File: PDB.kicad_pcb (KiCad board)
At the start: 2 copper layers, 63 parts, among them J1 Conn_02x03_Odd_Even, J2 USB_C_Receptacle_USB2.0, U1 ATmega2560-16AU, U2 LMZ13608, U3 LTC2946, U4 LTC2946, U5 FT230XQ, U6 Si8621, Y1 16MHz

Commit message: layout WIP
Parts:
- added C23: XT-F, XT30:XT30PW-F, F.Cu at (181.5, 66.5)
- added C24: XT-F, XT30:XT30PW-F, F.Cu at (199.0, 65.5)
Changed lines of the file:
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@@
     (tracks 177)
     (zones 0)
-    (modules 63)
+    (modules 65)
     (nets 138)
   )
@@
     (add_net "Net-(U5-Pad9)")
   )
+  (module XT30:XT30PW-F (layer F.Cu)
+    (at 199 65.5)
+    (fp_text reference C24 (at 0 18) (layer F.SilkS)
+      (effects (font (size 1 1) (thickness 0.15)))
+    )
+    (fp_text value XT-F (at 0 10) (layer F.Fab)
+      (effects (font (size 1 1) (thickness 0.15)))
+    )
+    (fp_line (start 4.5 6) (end 4.95 6) (layer F.Fab) (width 0.05))
+    (fp_line (start 4.5 0) (end 4.5 6) (layer F.Fab) (width 0.05))
+    (fp_line (start -4.5 6) (end -4.95 6) (layer F.Fab) (width 0.05))
+    (fp_line (start -4.5 0) (end -4.5 6) (layer F.Fab) (width 0.05))
+    (fp_text user REF** (at 0 8.5) (layer F.Fab)
+      (effects (font (size 1 1) (thickness 0.15)))
+    )
+    (fp_line (start 5 13) (end 5 17.1) (layer F.CrtYd) (width 0.05))
+    (fp_line (start 6.75 13) (end 5 13) (layer F.CrtYd) (width 0.05))
+    (fp_line (start -5 13) (end -6.75 13) (layer F.CrtYd) (width 0.05))
+    (fp_line (start -5 17.1) (end -5 13) (layer F.CrtYd) (width 0.05))
+    (fp_line (start -4.95 7.9) (end -5.5 7.9) (layer F.Fab) (width 0.05))
+    (fp_line (start -4.95 10.2) (end -5.5 10.2) (layer F.Fab) (width 0.05))
+    (fp_arc (start -5.5 9.05) (end -5.5 7.9) (angle -180) (layer F.Fab) (width 0.05))
+    (fp_line (start 4.95 10.2) (end 5.5 10.2) (layer F.Fab) (width 0.05))
+    (fp_line (start 4.95 7.9) (end 5.5 7.9) (layer F.Fab) (width 0.05))
+    (fp_arc (start 5.5 9.05) (end 5.5 10.2) (angle -180) (layer F.Fab) (width 0.05))
+    (fp_arc (start 2.5 14.05) (end 1.65 14.05) (angle -180) (layer F.Fab) (width 0.05))
+    (fp_arc (start -2.5 14.05) (end -3.35 14.05) (angle -180) (layer F.Fab) (width 0.05))
+    (fp_line (start 3.35 11) (end 3.35 14.05) (layer F.Fab) (width 0.05))
+    (fp_line (start 1.65 11) (end 1.65 14.05) (layer F.Fab) (width 0.05))
+    (fp_line (start -1.65 11) (end -1.65 14.05) (layer F.Fab) (width 0.05))
+    (fp_line (start -3.35 11) (end -3.35 14.05) (layer F.Fab) (width 0.05))
+    (fp_line (start -4.95 11) (end -4.95 6) (layer F.Fab) (width 0.05))
+    (fp_line (start 4.95 11) (end -4.95 11) (layer F.Fab) (width 0.05))
+    (fp_line (start 4.95 6) (end 4.95 11) (layer F.Fab) (width 0.05))
+    (fp_line (start -4.5 0) (end 4.5 0) (layer F.Fab) (width 0.05))
+    (fp_line (start -6.75 13) (end -6.75 -0.5) (layer F.CrtYd) (width 0.05))
+    (fp_line (start 5 17.1) (end -5 17.1) (layer F.CrtYd) (width 0.05))
+    (fp_line (start 6.75 -0.5) (end 6.75 13) (layer F.CrtYd) (width 0.05))
+    (fp_line (start -6.75 -0.5) (end 6.75 -0.5) (layer F.CrtYd) (width 0.05))
+    (pad 4 thru_hole circle (at 5.5 9.05) (size 2 2) (drill 1) (layers *.Cu *.Mask)
+      (net 1 GND))
+    (pad 3 thru_hole circle (at -5.5 9.05) (size 2 2) (drill 1) (layers *.Cu *.Mask)
+      (net 1 GND))
+    (pad 1 thru_hole circle (at 2.5 14.05) (size 3 3) (drill 1.7) (layers *.Cu *.Mask)
+      (net 43 +5V))
+    (pad 2 thru_hole circle (at -2.5 14.05) (size 3 3) (drill 1.7) (layers *.Cu *.Mask)
+      (net 1 GND))
+    (model ${KIPRJMOD}/ottojo_KicadLibs/XT30.pretty/XT30PW-F.stp
+      (offset (xyz 0 -8.300000000000001 0))
+      (scale (xyz 1 1 1))
+      (rotate (xyz 0 0 90))
+    )
+  )
+  (module XT30:XT30PW-F (layer F.Cu)
+    (at 181.5 66.5)
+    (fp_text reference C23 (at 0 18) (layer F.SilkS)
+      (effects (font (size 1 1) (thickness 0.15)))
+    )
+    (fp_text value XT-F (at 0 10) (layer F.Fab)
+      (effects (font (size 1 1) (thickness 0.15)))
+    )
+    (fp_line (start 4.5 6) (end 4.95 6) (layer F.Fab) (width 0.05))
+    (fp_line (start 4.5 0) (end 4.5 6) (layer F.Fab) (width 0.05))
+    (fp_line (start -4.5 6) (end -4.95 6) (layer F.Fab) (width 0.05))
+    (fp_line (start -4.5 0) (end -4.5 6) (layer F.Fab) (width 0.05))
+    (fp_text user REF** (at 0 8.5) (layer F.Fab)
+      (effects (font (size 1 1) (thickness 0.15)))
+    )
+    (fp_line (start 5 13) (end 5 17.1) (layer F.CrtYd) (width 0.05))
+    (fp_line (start 6.75 13) (end 5 13) (layer F.CrtYd) (width 0.05))
+    (fp_line (start -5 13) (end -6.75 13) (layer F.CrtYd) (width 0.05))
+    (fp_line (start -5 17.1) (end -5 13) (layer F.CrtYd) (width 0.05))
+    (fp_line (start -4.95 7.9) (end -5.5 7.9) (layer F.Fab) (width 0.05))
+    (fp_line (start -4.95 10.2) (end -5.5 10.2) (layer F.Fab) (width 0.05))
+    (fp_arc (start -5.5 9.05) (end -5.5 7.9) (angle -180) (layer F.Fab) (width 0.05))
+    (fp_line (start 4.95 10.2) (end 5.5 10.2) (layer F.Fab) (width 0.05))
+    (fp_line (start 4.95 7.9) (end 5.5 7.9) (layer F.Fab) (width 0.05))
+    (fp_arc (start 5.5 9.05) (end 5.5 10.2) (angle -180) (layer F.Fab) (width 0.05))
+    (fp_arc (start 2.5 14.05) (end 1.65 14.05) (angle -180) (layer F.Fab) (width 0.05))
+    (fp_arc (start -2.5 14.05) (end -3.35 14.05) (angle -180) (layer F.Fab) (width 0.05))
+    (fp_line (start 3.35 11) (end 3.35 14.05) (layer F.Fab) (width 0.05))
+    (fp_line (start 1.65 11) (end 1.65 14.05) (layer F.Fab) (width 0.05))
+    (fp_line (start -1.65 11) (end -1.65 14.05) (layer F.Fab) (width 0.05))
+    (fp_line (start -3.35 11) (end -3.35 14.05) (layer F.Fab) (width 0.05))
+    (fp_line (start -4.95 11) (end -4.95 6) (layer F.Fab) (width 0.05))
+    (fp_line (start 4.95 11) (end -4.95 11) (layer F.Fab) (width 0.05))
+    (fp_line (start 4.95 6) (end 4.95 11) (layer F.Fab) (width 0.05))
+    (fp_line (start -4.5 0) (end 4.5 0) (layer F.Fab) (width 0.05))
+    (fp_line (start -6.75 13) (end -6.75 -0.5) (layer F.CrtYd) (width 0.05))
+    (fp_line (start 5 17.1) (end -5 17.1) (layer F.CrtYd) (width 0.05))
+    (fp_line (start 6.75 -0.5) (end 6.75 13) (layer F.CrtYd) (width 0.05))
+    (fp_line (start -6.75 -0.5) (end 6.75 -0.5) (layer F.CrtYd) (width 0.05))
+    (pad 4 thru_hole circle (at 5.5 9.05) (size 2 2) (drill 1) (layers *.Cu *.Mask)
+      (net 1 GND))
+    (pad 3 thru_hole circle (at -5.5 9.05) (size 2 2) (drill 1) (layers *.Cu *.Mask)
+      (net 1 GND))
+    (pad 1 thru_hole circle (at 2.5 14.05) (size 3 3) (drill 1.7) (layers *.Cu *.Mask)
+      (net 43 +5V))
+    (pad 2 thru_hole circle (at -2.5 14.05) (size 3 3) (drill 1.7) (layers *.Cu *.Mask)
+      (net 1 GND))
+    (model ${KIPRJMOD}/ottojo_KicadLibs/XT30.pretty/XT30PW-F.stp
+      (offset (xyz 0 -8.300000000000001 0))
+      (scale (xyz 1 1 1))
+      (rotate (xyz 0 0 90))
+    )
+  )
   (module XT60:XT60PW-F (layer F.Cu)
     (at 98 65)
@@
       (effects (font (size 1 1) (thickness 0.15)))
     )
+    (fp_line (start -5 -1.75) (end 5 -1.75) (layer F.Fab) (width 0.1))
+    (fp_line (start -8 9) (end -8 -11) (layer F.CrtYd) (width 0.05))
+    (fp_line (start 8 9) (end -8 9) (layer F.CrtYd) (width 0.05))
+    (fp_line (start 8 -11) (end 8 9) (layer F.CrtYd) (width 0.05))
     (fp_line (start -8 -11) (end 8 -11) (layer F.CrtYd) (width 0.05))
-    (fp_line (start 8 -11) (end 8 9) (layer F.CrtYd) (width 0.05))
-    (fp_line (start 8 9) (end -8 9) (layer F.CrtYd) (width 0.05))
-    (fp_line (start -8 9) (end -8 -11) (layer F.CrtYd) (width 0.05))
-    (fp_line (start -5 -1.75) (end 5 -1.75) (layer F.Fab) (width 0.1))
-    (pad 4 thru_hole oval (at 6.75 0 90) (size 2.9 1.3) (drill oval 2.3 0.7) (layers *.Cu *.Mask)
-      (net 1 GND))
-    (pad 3 thru_hole oval (at -6.75 0 90) (size 2.9 1.3) (drill oval 2.3 0.7) (layers *.Cu *.Mask)
-      (net 1 GND))
-    (pad 2 thru_hole circle (at 3.6 6 90) (size 4.5 4.5) (drill 2.8) (layers *.Cu *.Mask)
-      (net 1 GND))
     (pad 1 thru_hole circle (at -3.6 6) (size 4.5 4.5) (drill 2.8) (layers *.Cu *.Mask)
       (net 5 /BAT/VBATOUT))
+    (pad 2 thru_hole circle (at 3.6 6 90) (size 4.5 4.5) (drill 2.8) (layers *.Cu *.Mask)
+      (net 1 GND))
+    (pad 3 thru_hole oval (at -6.75 0 90) (size 2.9 1.3) (drill oval 2.3 0.7) (layers *.Cu *.Mask)
+      (net 1 GND))
+    (pad 4 thru_hole oval (at 6.75 0 90) (size 2.9 1.3) (drill oval 2.3 0.7) (layers *.Cu *.Mask)
+      (net 1 GND))
     (model ${KIPRJMOD}/ottojo_KicadLibs/XT60.pretty/XT60PW-F.stp
       (offset (xyz 0 9.35 4.2))
@@
       (effects (font (size 1 1) (thickness 0.15)))
     )
+    (fp_line (start -5 -1.75) (end 5 -1.75) (layer F.Fab) (width 0.1))
+    (fp_line (start -8 9) (end -8 -11) (layer F.CrtYd) (width 0.05))
+    (fp_line (start 8 9) (end -8 9) (layer F.CrtYd) (width 0.05))
+    (fp_line (start 8 -11) (end 8 9) (layer F.CrtYd) (width 0.05))
     (fp_line (start -8 -11) (end 8 -11) (layer F.CrtYd) (width 0.05))
-    (fp_line (start 8 -11) (end 8 9) (layer F.CrtYd) (width 0.05))
-    (fp_line (start 8 9) (end -8 9) (layer F.CrtYd) (width 0.05))
-    (fp_line (start -8 9) (end -8 -11) (layer F.CrtYd) (width 0.05))
-    (fp_line (start -5 -1.75) (end 5 -1.75) (layer F.Fab) (width 0.1))
-    (pad 4 thru_hole oval (at 6.75 0 90) (size 2.9 1.3) (drill oval 2.3 0.7) (layers *.Cu *.Mask)
-      (net 1 GND))
-    (pad 3 thru_hole oval (at -6.75 0 90) (size 2.9 1.3) (drill oval 2.3 0.7) (layers *.Cu *.Mask)
+    (pad 1 thru_hole circle (at -3.6 6) (size 4.5 4.5) (drill 2.8) (layers *.Cu *.Mask)
       (net 1 GND))
     (pad 2 thru_hole circle (at 3.6 6 90) (size 4.5 4.5) (drill 2.8) (layers *.Cu *.Mask)
       (net 6 /BAT/VBATIN))
-    (pad 1 thru_hole circle (at -3.6 6) (size 4.5 4.5) (drill 2.8) (layers *.Cu *.Mask)
+    (pad 3 thru_hole oval (at -6.75 0 90) (size 2.9 1.3) (drill oval 2.3 0.7) (layers *.Cu *.Mask)
+      (net 1 GND))
+    (pad 4 thru_hole oval (at 6.75 0 90) (size 2.9 1.3) (drill oval 2.3 0.7) (layers *.Cu *.Mask)
       (net 1 GND))
     (model ${KIPRJMOD}/ottojo_KicadLibs/XT60.pretty/XT60PW-M.stp

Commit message: layout wip
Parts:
- added J3: USB_C_Receptacle_USB2.0, GT-USB-7010:USB_C_Receptacle_GT-USB-7010, F.Cu at (133.1, 137.7)
- added R26: 10k, Resistor_SMD:R_0603_1608Metric, F.Cu at (139.6, 135.3)
- added R27: 10k, Resistor_SMD:R_0603_1608Metric, F.Cu at (139.6, 133.8)
- moved R9 176.1 mm to (81.5, 120.0)
- moved R8 172.3 mm to (81.2, 117.0)
- moved C24 139.9 mm to (60.0, 81.0), turned to 90 degrees
- moved R11 126.9 mm to (84.5, 141.3)
- moved R10 124.1 mm to (84.5, 137.5)
- moved C23 123.3 mm to (65.0, 107.0), turned to 90 degrees
- moved J1 106.3 mm to (90.0, 141.0), turned to 90 degrees
- moved R7 93.8 mm to (105.0, 131.5)
- moved A1 86.3 mm to (106.9, 136.1)
- moved C10 86.3 mm to (106.8, 141.0)
- moved C12 86.3 mm to (101.5, 135.9)
- moved R12 86.3 mm to (111.0, 138.5)
- moved R13 86.3 mm to (111.0, 135.3)
- moved R1 42.9 mm to (73.2, 92.0)
- moved R2 39.8 mm to (69.0, 92.0)
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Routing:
- added copper zone on B.Cu, net GND
- added copper zone on F.Cu, net GND
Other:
- board outline added: 50 x 90 mm

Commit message: wip und so
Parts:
- removed C1: XT-M, XT60:XT60PW-M
- removed C20: XT-F, XT60:XT60PW-F
- removed C23, C24: XT-F, XT30:XT30PW-F
- removed R26, R27: 10k, Resistor_SMD:R_0603_1608Metric
- added J4: Conn_01x02, XT30:XT30PB-F, F.Cu at (127.0, 133.2)
- added J5: Conn_01x02, XT30:XT30PB-F, F.Cu at (139.2, 126.0)
- added J6: Conn_01x02, XT60:XT60PB-M, F.Cu at (-11.0, 34.0)
- added J7: Conn_01x02_MountingPin, XT60:XT60PW-F, F.Cu at (8.03, 11.0)
- J3: value USB_C_Receptacle_USB2.0 -> Conn_01x02; footprint GT-USB-7010:USB_C_Receptacle_GT-USB-7010 -> XT30:XT30PB-F
- moved C10 80.4 mm to (185.8, 126.0)
- moved C12 80.4 mm to (180.5, 120.9)
- moved C2 80.4 mm to (188.0, 106.0)
- moved C3 80.4 mm to (188.0, 114.5)
- moved C4 80.4 mm to (174.0, 117.8)
- moved C5 80.4 mm to (165.0, 112.2)
- moved C6 80.4 mm to (176.5, 98.2)
- moved C7 80.4 mm to (165.0, 104.8)
- moved C8 80.4 mm to (184.2, 112.2)
- moved D1 80.4 mm to (190.2, 99.0)
- moved D2 80.4 mm to (190.2, 96.0)
- moved D3 80.4 mm to (190.2, 93.0)
- moved D4 80.4 mm to (190.2, 90.0)
- moved J1 80.4 mm to (169.0, 126.0)
- moved R10 80.4 mm to (163.5, 122.5)
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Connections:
- A1 pad 5: Net-(A1-Pad5) -> (no net)
- J2 pad A8: Net-(J2-PadA8) -> (no net)
- J2 pad B8: Net-(J2-PadB8) -> (no net)
- U1 pad 1: Net-(U1-Pad1) -> (no net)
- U1 pad 12: Net-(U1-Pad12) -> (no net)
- U1 pad 13: Net-(U1-Pad13) -> (no net)
- U1 pad 14: Net-(U1-Pad14) -> (no net)
- U1 pad 15: Net-(U1-Pad15) -> (no net)
- U1 pad 16: Net-(U1-Pad16) -> (no net)
- U1 pad 17: Net-(U1-Pad17) -> (no net)
- U1 pad 18: Net-(U1-Pad18) -> (no net)
- U1 pad 19: Net-(U1-Pad19) -> (no net)
- U1 pad 23: Net-(U1-Pad23) -> (no net)
- U1 pad 24: Net-(U1-Pad24) -> (no net)
- U1 pad 25: Net-(U1-Pad25) -> (no net)
- U1 pad 26: Net-(U1-Pad26) -> (no net)
- U1 pad 27: Net-(U1-Pad27) -> (no net)
- U1 pad 28: Net-(U1-Pad28) -> (no net)
- U1 pad 29: Net-(U1-Pad29) -> (no net)
- U1 pad 39: Net-(U1-Pad39) -> (no net)
- U1 pad 4: Net-(U1-Pad4) -> (no net)
- U1 pad 40: Net-(U1-Pad40) -> (no net)
- U1 pad 41: Net-(U1-Pad41) -> (no net)
- U1 pad 42: Net-(U1-Pad42) -> (no net)
- U1 pad 45: Net-(U1-Pad45) -> (no net)
- U1 pad 46: Net-(U1-Pad46) -> (no net)
- U1 pad 47: Net-(U1-Pad47) -> (no net)
- U1 pad 48: Net-(U1-Pad48) -> (no net)
- U1 pad 49: Net-(U1-Pad49) -> (no net)
- U1 pad 5: Net-(U1-Pad5) -> (no net)
- U1 pad 50: Net-(U1-Pad50) -> (no net)
- U1 pad 51: Net-(U1-Pad51) -> (no net)
- U1 pad 52: Net-(U1-Pad52) -> (no net)
- U1 pad 53: Net-(U1-Pad53) -> (no net)
- U1 pad 54: Net-(U1-Pad54) -> (no net)
- U1 pad 55: Net-(U1-Pad55) -> (no net)
- U1 pad 56: Net-(U1-Pad56) -> (no net)
- U1 pad 57: Net-(U1-Pad57) -> (no net)
- U1 pad 58: Net-(U1-Pad58) -> (no net)
- U1 pad 59: Net-(U1-Pad59) -> (no net)
- U1 pad 60: Net-(U1-Pad60) -> (no net)
- U1 pad 63: Net-(U1-Pad63) -> (no net)
- U1 pad 64: Net-(U1-Pad64) -> (no net)
- U1 pad 65: Net-(U1-Pad65) -> (no net)
- U1 pad 66: Net-(U1-Pad66) -> (no net)
- U1 pad 67: Net-(U1-Pad67) -> (no net)
- U1 pad 68: Net-(U1-Pad68) -> (no net)
- U1 pad 69: Net-(U1-Pad69) -> (no net)
- U1 pad 70: Net-(U1-Pad70) -> (no net)
- U1 pad 71: Net-(U1-Pad71) -> (no net)
- U1 pad 72: Net-(U1-Pad72) -> (no net)
- U1 pad 73: Net-(U1-Pad73) -> (no net)
- U1 pad 74: Net-(U1-Pad74) -> (no net)
- U1 pad 75: Net-(U1-Pad75) -> (no net)
- U1 pad 76: Net-(U1-Pad76) -> (no net)
- U1 pad 77: Net-(U1-Pad77) -> (no net)
- U1 pad 78: Net-(U1-Pad78) -> (no net)
- U1 pad 79: Net-(U1-Pad79) -> (no net)
- U1 pad 8: Net-(U1-Pad8) -> (no net)
- U1 pad 82: Net-(U1-Pad82) -> (no net)
- U1 pad 83: Net-(U1-Pad83) -> (no net)
- U1 pad 84: Net-(U1-Pad84) -> (no net)
- U1 pad 85: Net-(U1-Pad85) -> (no net)
- U1 pad 86: Net-(U1-Pad86) -> (no net)
- U1 pad 87: Net-(U1-Pad87) -> (no net)
- U1 pad 88: Net-(U1-Pad88) -> (no net)
- U1 pad 89: Net-(U1-Pad89) -> (no net)
- U1 pad 9: Net-(U1-Pad9) -> (no net)
- U1 pad 90: Net-(U1-Pad90) -> (no net)
- U1 pad 91: Net-(U1-Pad91) -> (no net)
- U1 pad 92: Net-(U1-Pad92) -> (no net)
- U1 pad 93: Net-(U1-Pad93) -> (no net)
- U1 pad 94: Net-(U1-Pad94) -> (no net)
- U1 pad 95: Net-(U1-Pad95) -> (no net)
- U1 pad 96: Net-(U1-Pad96) -> (no net)
- U1 pad 97: Net-(U1-Pad97) -> (no net)
- U2 pad 4: Net-(U2-Pad4) -> (no net)
- U2 pad 8: Net-(U2-Pad8) -> (no net)
- U2 pad 9: Net-(U2-Pad9) -> (no net)
- U3 pad 10: Net-(U3-Pad10) -> (no net)
- U3 pad 13: Net-(U3-Pad13) -> (no net)
- U3 pad 3: Net-(U3-Pad3) -> (no net)
- U3 pad 4: Net-(U3-Pad4) -> (no net)
- U4 pad 10: Net-(U4-Pad10) -> (no net)
- U4 pad 13: Net-(U4-Pad13) -> (no net)
- U4 pad 3: Net-(U4-Pad3) -> (no net)
- U4 pad 4: Net-(U4-Pad4) -> (no net)
- U5 pad 12: Net-(U5-Pad12) -> (no net)
- U5 pad 14: Net-(U5-Pad14) -> (no net)
- U5 pad 16: Net-(U5-Pad16) -> (no net)
- U5 pad 4: Net-(U5-Pad4) -> (no net)
- U5 pad 9: Net-(U5-Pad9) -> (no net)
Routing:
- net Net-(C14-Pad1): track 12.8 -> 0.00 mm
- net Net-(D6-Pad1): track 20.3 -> 9.91 mm, vias 2 -> 0
- net +5V: track 8.85 -> 0.00 mm
- net Net-(D5-Pad1): track 18.8 -> 14.7 mm, vias 2 -> 0
- net Net-(C18-Pad1): track 2.12 -> 0.00 mm

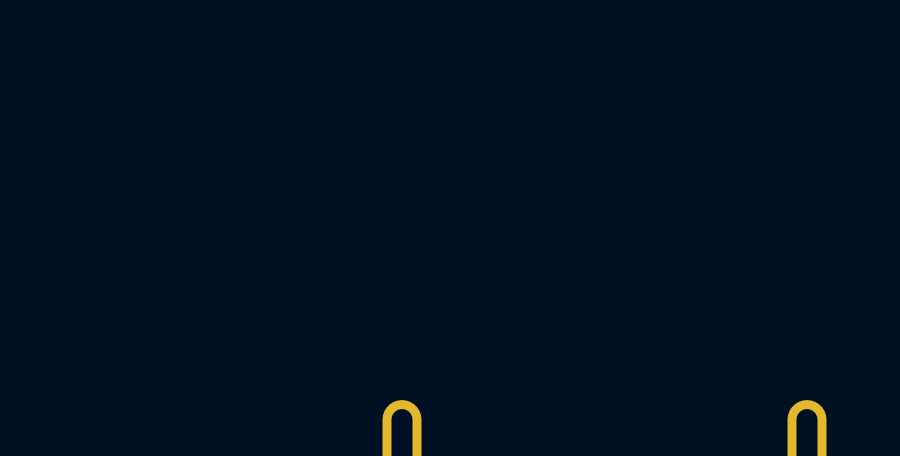
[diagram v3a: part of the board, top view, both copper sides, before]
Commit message: add reset switch
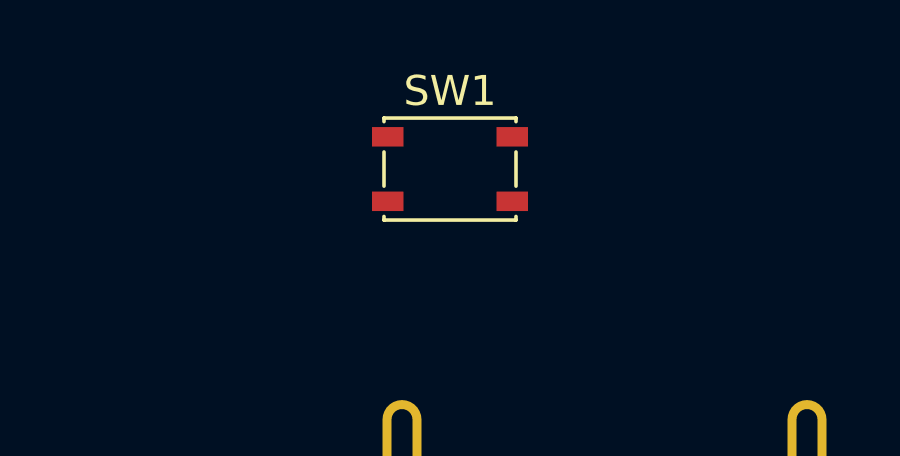
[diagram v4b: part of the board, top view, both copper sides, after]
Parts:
- added SW1: SW_Push, Button_Switch_SMD:SW_SPST_PTS810, F.Cu at (2.88, 1.88)
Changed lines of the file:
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@@
     (tracks 160)
     (zones 0)
-    (modules 66)
+    (modules 67)
     (nets 47)
   )
@@
     (add_net "Net-(R6-Pad1)")
   )
+  (module Button_Switch_SMD:SW_SPST_PTS810 (layer F.Cu)
+    (at 2.875001 1.875001)
+    (descr "C&K Components, PTS 810 Series, Microminiature SMT Top Actuated, http://www.ckswitches.com/media/1476/pts810.pdf")
+    (tags "SPST Button Switch")
+    (attr smd)
+    (fp_text reference SW1 (at 0 -2.6) (layer F.SilkS)
+      (effects (font (size 1 1) (thickness 0.15)))
+    )
+    (fp_text value SW_Push (at 0 2.6) (layer F.Fab)
+      (effects (font (size 1 1) (thickness 0.15)))
+    )
+    (fp_arc (start 0.4 0) (end 0.4 -1.1) (angle 180) (layer F.Fab) (width 0.1))
+    (fp_line (start 2.1 1.6) (end 2.1 -1.6) (layer F.Fab) (width 0.1))
+    (fp_line (start 2.1 -1.6) (end -2.1 -1.6) (layer F.Fab) (width 0.1))
+    (fp_line (start -2.1 -1.6) (end -2.1 1.6) (layer F.Fab) (width 0.1))
+    (fp_line (start -2.1 1.6) (end 2.1 1.6) (layer F.Fab) (width 0.1))
+    (fp_arc (start -0.4 0) (end -0.4 1.1) (angle 180) (layer F.Fab) (width 0.1))
+    (fp_line (start -0.4 -1.1) (end 0.4 -1.1) (layer F.Fab) (width 0.1))
+    (fp_line (start 0.4 1.1) (end -0.4 1.1) (layer F.Fab) (width 0.1))
+    (fp_line (start 2.2 -1.7) (end -2.2 -1.7) (layer F.SilkS) (width 0.12))
+    (fp_line (start -2.2 -1.7) (end -2.2 -1.58) (layer F.SilkS) (width 0.12))
+    (fp_line (start -2.2 -0.57) (end -2.2 0.57) (layer F.SilkS) (width 0.12))
+    (fp_line (start -2.2 1.58) (end -2.2 1.7) (layer F.SilkS) (width 0.12))
+    (fp_line (start -2.2 1.7) (end 2.2 1.7) (layer F.SilkS) (width 0.12))
+    (fp_line (start 2.2 1.7) (end 2.2 1.58) (layer F.SilkS) (width 0.12))
+    (fp_line (start 2.2 0.57) (end 2.2 -0.57) (layer F.SilkS) (width 0.12))
+    (fp_line (start 2.2 -1.58) (end 2.2 -1.7) (layer F.SilkS) (width 0.12))
+    (fp_text user %R (at 0 0) (layer F.Fab)
+      (effects (font (size 0.6 0.6) (thickness 0.09)))
+    )
+    (fp_line (start 2.85 -1.85) (end 2.85 1.85) (layer F.CrtYd) (width 0.05))
+    (fp_line (start 2.85 1.85) (end -2.85 1.85) (layer F.CrtYd) (width 0.05))
+    (fp_line (start -2.85 1.85) (end -2.85 -1.85) (layer F.CrtYd) (width 0.05))
+    (fp_line (start -2.85 -1.85) (end 2.85 -1.85) (layer F.CrtYd) (width 0.05))
+    (pad 2 smd rect (at 2.075 1.075) (size 1.05 0.65) (layers F.Cu F.Paste F.Mask)
+      (net 25 /ATMega/~RESET~))
+    (pad 2 smd rect (at -2.075 1.075) (size 1.05 0.65) (layers F.Cu F.Paste F.Mask)
+      (net 25 /ATMega/~RESET~))
+    (pad 1 smd rect (at 2.075 -1.075) (size 1.05 0.65) (layers F.Cu F.Paste F.Mask)
+      (net 1 GND))
+    (pad 1 smd rect (at -2.075 -1.075) (size 1.05 0.65) (layers F.Cu F.Paste F.Mask)
+      (net 1 GND))
+    (model ${KISYS3DMOD}/Button_Switch_SMD.3dshapes/SW_SPST_PTS810.wrl
+      (at (xyz 0 0 0))
+      (scale (xyz 1 1 1))
+      (rotate (xyz 0 0 0))
+    )
+  )
   (module XT60:XT60PB-M (layer F.Cu)
